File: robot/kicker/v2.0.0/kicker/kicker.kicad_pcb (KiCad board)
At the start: 4 copper layers, 76 x 90 mm, 128 parts, among them J1 XT30PW-M, J2 1054052108, J3 2157601002, J4 2157601002, J5 Conn_ARM_JTAG_SWD_10, J6 Conn_01x03_Female, J7 Conn_01x03, J8 Conn_01x03, Q1 BSC0402NSATMA1, Q2 IXGA48N60A3, Q3 IXGA48N60A3, Q4 BSS138K, U1 LM1117-5.0, U2 LM1117-3.3, U3 ADUM7441, U4 LT3757EMSE, U5 IX4427, U6 STM32F030K6Tx, U7 SK9822, U8 SK9822

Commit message: small resistor tweak
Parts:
- R26: value 16k2 0%1 -> 17k4 0%1

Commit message: Diode & Rsense update; minor ERC fixes
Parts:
- D9: value MURS460 -> HS5M
- R22, R23: value 8m00 1% -> 4m00 1%
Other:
- board text added: "Kicker v2.0.0"
- board text removed: "Kicker v1.1.0"
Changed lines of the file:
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@@
   (net 2 "GND")
   (net 3 "+5V")
-  (net 4 "Net-(#FLG04-pwr)")
+  (net 4 "Net-(D4-K)")
   (net 5 "/flyback_charger/V_{solenoid}")
   (net 6 "VBUS")
@@
         (effects (font (size 1 1) (thickness 0.15)))
     )
-    (fp_text value "MURS460" (at 0 4.2) (layer "F.Fab")
+    (fp_text value "HS5M" (at 0 4.2) (layer "F.Fab")
         (effects (font (size 1 1) (thickness 0.15)))
     )
@@
       (stroke (width 0.05) (type solid)) (layer "F.CrtYd"))
     (pad "1" smd rect (at -10 15.475 90) (size 2 2.75) (layers "F.Cu" "F.Paste" "F.Mask")
-      (net 8 "/flyback_charger/V_{trans}") (pintype "bidirectional"))
+      (net 8 "/flyback_charger/V_{trans}") (pintype "passive"))
     (pad "2" smd rect (at -6 15.475 90) (size 2 2.75) (layers "F.Cu" "F.Paste" "F.Mask")
-      (net 8 "/flyback_charger/V_{trans}") (pintype "bidirectional"))
+      (net 8 "/flyback_charger/V_{trans}") (pintype "passive"))
     (pad "3" smd rect (at -2 15.475 90) (size 2 2.75) (layers "F.Cu" "F.Paste" "F.Mask")
-      (net 8 "/flyback_charger/V_{trans}") (pintype "bidirectional"))
+      (net 8 "/flyback_charger/V_{trans}") (pintype "passive"))
     (pad "4" smd rect (at 2 15.475 90) (size 2 2.75) (layers "F.Cu" "F.Paste" "F.Mask")
-      (net 8 "/flyback_charger/V_{trans}") (pintype "bidirectional"))
+      (net 8 "/flyback_charger/V_{trans}") (pintype "passive"))
     (pad "5" smd rect (at 6 15.475 90) (size 2 2.75) (layers "F.Cu" "F.Paste" "F.Mask")
       (net 78 "unconnected-(L1-Pad5)") (pintype "no_connect"))
     (pad "6" smd rect (at 10 15.475 90) (size 2 2.75) (layers "F.Cu" "F.Paste" "F.Mask")
-      (net 2 "GND") (pintype "bidirectional"))
+      (net 2 "GND") (pintype "passive"))
     (pad "7" smd rect (at 10 -15.475 90) (size 2 2.75) (layers "F.Cu" "F.Paste" "F.Mask")
-      (net 64 "/flyback_charger/HV_AC") (pintype "bidirectional"))
+      (net 64 "/flyback_charger/HV_AC") (pintype "passive"))
     (pad "8" smd rect (at 6 -15.475 90) (size 2 2.75) (layers "F.Cu" "F.Paste" "F.Mask")
       (net 79 "unconnected-(L1-Pad8)") (pintype "no_connect"))
     (pad "9" smd rect (at 2 -15.475 90) (size 2 2.75) (layers "F.Cu" "F.Paste" "F.Mask")
-      (net 7 "+BATT") (pintype "bidirectional"))
+      (net 7 "+BATT") (pintype "passive"))
     (pad "10" smd rect (at -2 -15.475 90) (size 2 2.75) (layers "F.Cu" "F.Paste" "F.Mask")
-      (net 7 "+BATT") (pintype "bidirectional"))
+      (net 7 "+BATT") (pintype "passive"))
     (pad "11" smd rect (at -6 -15.475 90) (size 2 2.75) (layers "F.Cu" "F.Paste" "F.Mask")
-      (net 7 "+BATT") (pintype "bidirectional"))
+      (net 7 "+BATT") (pintype "passive"))
     (pad "12" smd rect (at -10 -15.475 90) (size 2 2.75) (layers "F.Cu" "F.Paste" "F.Mask")
-      (net 7 "+BATT") (pintype "bidirectional"))
+      (net 7 "+BATT") (pintype "passive"))
   )
   (footprint "MountingHole:MountingHole_3.2mm_M3_ISO7380_Pad" (layer "F.Cu")
@@
         (effects (font (size 1 1) (thickness 0.15)))
     )
-    (fp_text value "8m00 1%" (at 0 1.82 90) (layer "F.Fab")
+    (fp_text value "4m00 1%" (at 0 1.82 90) (layer "F.Fab")
         (effects (font (size 1 1) (thickness 0.15)))
     )
@@
         (effects (font (size 1 1) (thickness 0.15)))
     )
-    (fp_text value "8m00 1%" (at 0 1.82 90) (layer "F.Fab")
+    (fp_text value "4m00 1%" (at 0 1.82 90) (layer "F.Fab")
         (effects (font (size 1 1) (thickness 0.15)))
     )
@@
       (net 11 "+3.3V") (pinfunction "VO") (pintype "power_out"))
     (pad "3" smd rect (at -3.15 -2.3 90) (size 2 1.5) (layers "B.Cu" "B.Paste" "B.Mask")
-      (net 4 "Net-(#FLG04-pwr)") (pinfunction "VI") (pintype "power_in"))
+      (net 4 "Net-(D4-K)") (pinfunction "VI") (pintype "power_in"))
     (model "${KICAD6_3DMODEL_DIR}/Package_TO_SOT_SMD.3dshapes/SOT-223.wrl"
       (offset (xyz 0 0 0))
@@
       (stroke (width 0.1) (type solid)) (layer "B.Fab"))
     (pad "1" smd roundrect (at -1.05 0 90) (size 0.6 0.45) (layers "B.Cu" "B.Paste" "B.Mask") (roundrect_rratio 0.25)
-      (net 4 "Net-(#FLG04-pwr)") (pinfunction "K") (pintype "passive"))
+      (net 4 "Net-(D4-K)") (pinfunction "K") (pintype "passive"))
     (pad "2" smd roundrect (at 1.05 0 90) (size 0.6 0.45) (layers "B.Cu" "B.Paste" "B.Mask") (roundrect_rratio 0.25)
       (net 11 "+3.3V") (pinfunction "A") (pintype "passive"))
@@
       (stroke (width 0.1) (type solid)) (layer "B.Fab"))
     (pad "1" smd roundrect (at -0.775 0 90) (size 0.9 0.95) (layers "B.Cu" "B.Paste" "B.Mask") (roundrect_rratio 0.25)
-      (net 4 "Net-(#FLG04-pwr)") (pintype "passive"))
+      (net 4 "Net-(D4-K)") (pintype "passive"))
     (pad "2" smd roundrect (at 0.775 0 90) (size 0.9 0.95) (layers "B.Cu" "B.Paste" "B.Mask") (roundrect_rratio 0.25)
       (net 2 "GND") (pintype "passive"))
@@
       (stroke (width 0.16) (type solid)) (fill solid) (layer "B.Mask"))
     (pad "1" smd custom (at -0.85 0 180) (size 0.3 0.3) (layers "B.Cu" "B.Mask")
-      (net 4 "Net-(#FLG04-pwr)") (pinfunction "A") (pintype "passive") (zone_connect 2) (thermal_bridge_angle 45)
+      (net 4 "Net-(D4-K)") (pinfunction "A") (pintype "passive") (zone_connect 2) (thermal_bridge_angle 45)
       (options (clearance outline) (anchor rect))
       (primitives
@@
   (gr_line (start 253 109) (end 253 108)
     (stroke (width 0.1) (type solid)) (layer "Edge.Cuts"))
-  (gr_text "Kicker v1.1.0" (at 235.1 147.5 90) (layer "F.SilkS")
+  (gr_text "Kicker v2.0.0" (at 235.1 147.5 90) (layer "F.SilkS")
     (effects (font (size 2 2) (thickness 0.3)))
   )

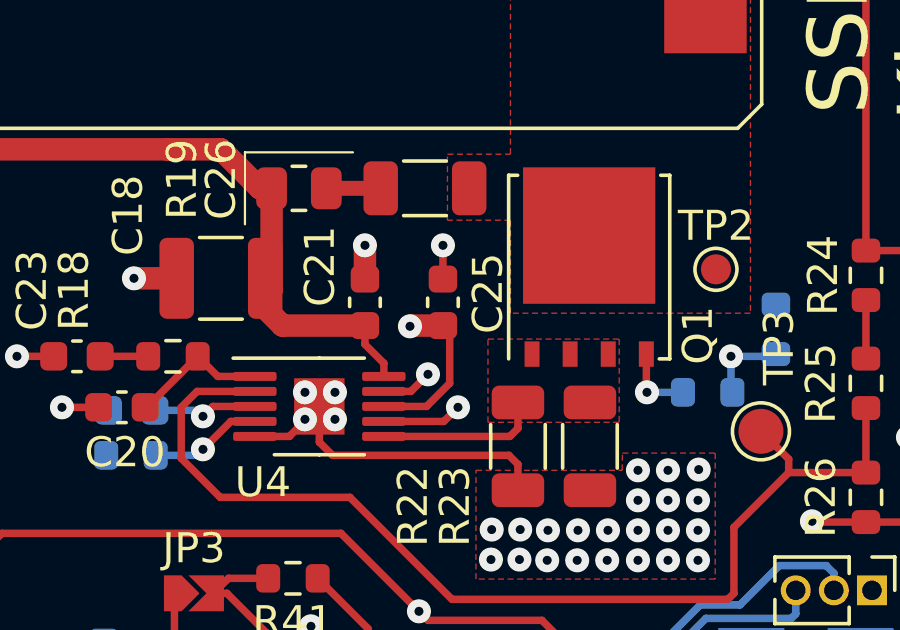
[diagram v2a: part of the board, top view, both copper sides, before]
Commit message: Consolidate 4.7uF capacitor variants into one BoM item
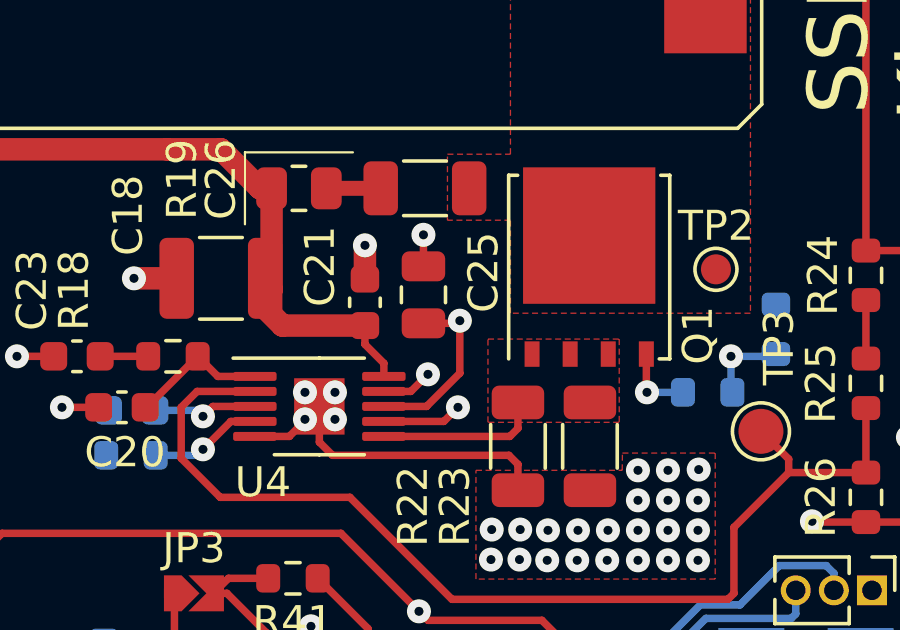
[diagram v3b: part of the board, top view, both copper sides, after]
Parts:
- C25: footprint Capacitor_SMD:C_0603_1608Metric -> Capacitor_SMD:C_0805_2012Metric
- C29, C34: value 4u7 25V -> 4u7 50V
- moved C25 0.70 mm to (218.2, 162.2)
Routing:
- net +12V: track 188.9 -> 187.4 mm
